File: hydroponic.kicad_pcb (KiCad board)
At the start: 2 copper layers, 110 x 80.3 mm, 102 parts, among them J1 12V DC, J10 Matrix key, J11 ds18b20, J12 ec, J13 bh1750, J14 dht11, J2 vi, J3 po, J4 pa, J5 pb, J6 vo, J7 fa, J8 lt, J9 lcd, U1 ULN2003, U10 LM324, U11 AMP4953, U12 AMP4953, U13 AMP4953, U14 LM324, U2 STM32duino, U3 LM2596T-5V, U4 AMP4953, U5 nodemcu, U6 LM1117-3.3, U7 AMP4953, U8 AMP4953, U9 AMP4953

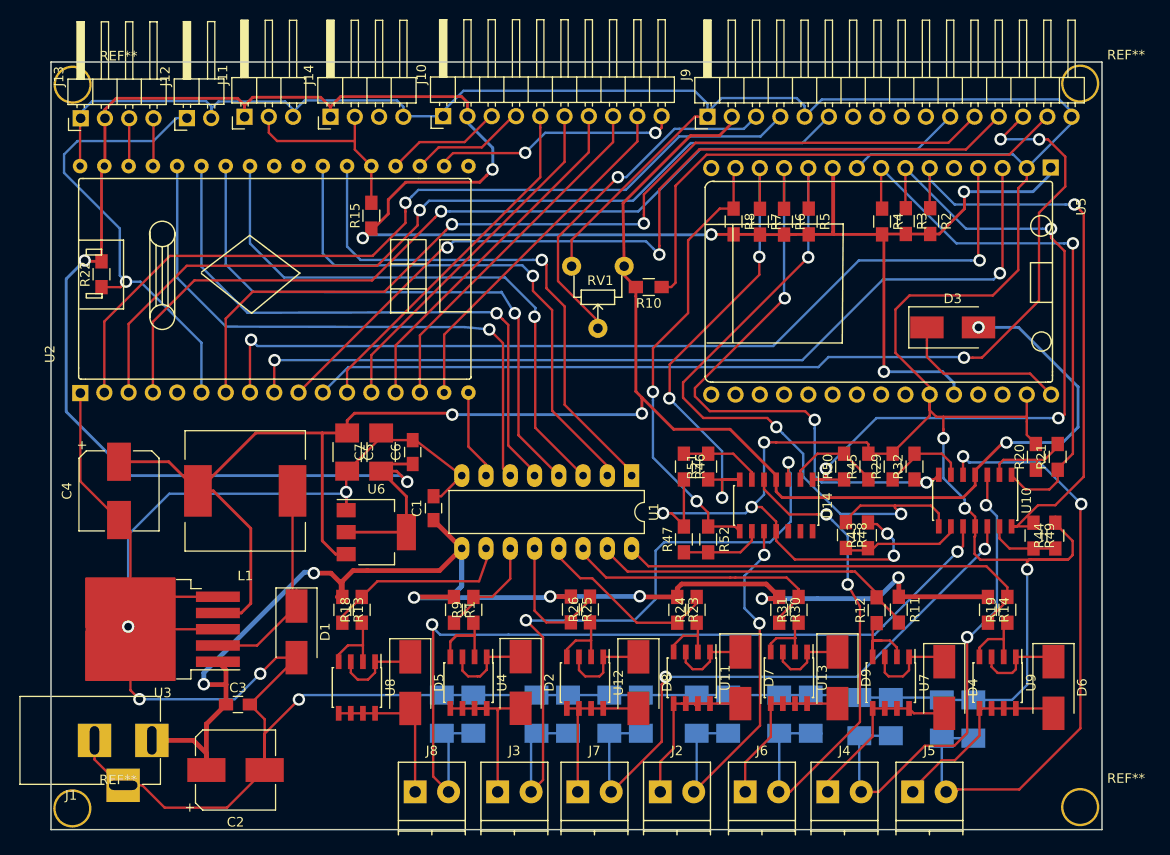
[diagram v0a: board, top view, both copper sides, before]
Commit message: add net 12v to AMP4953
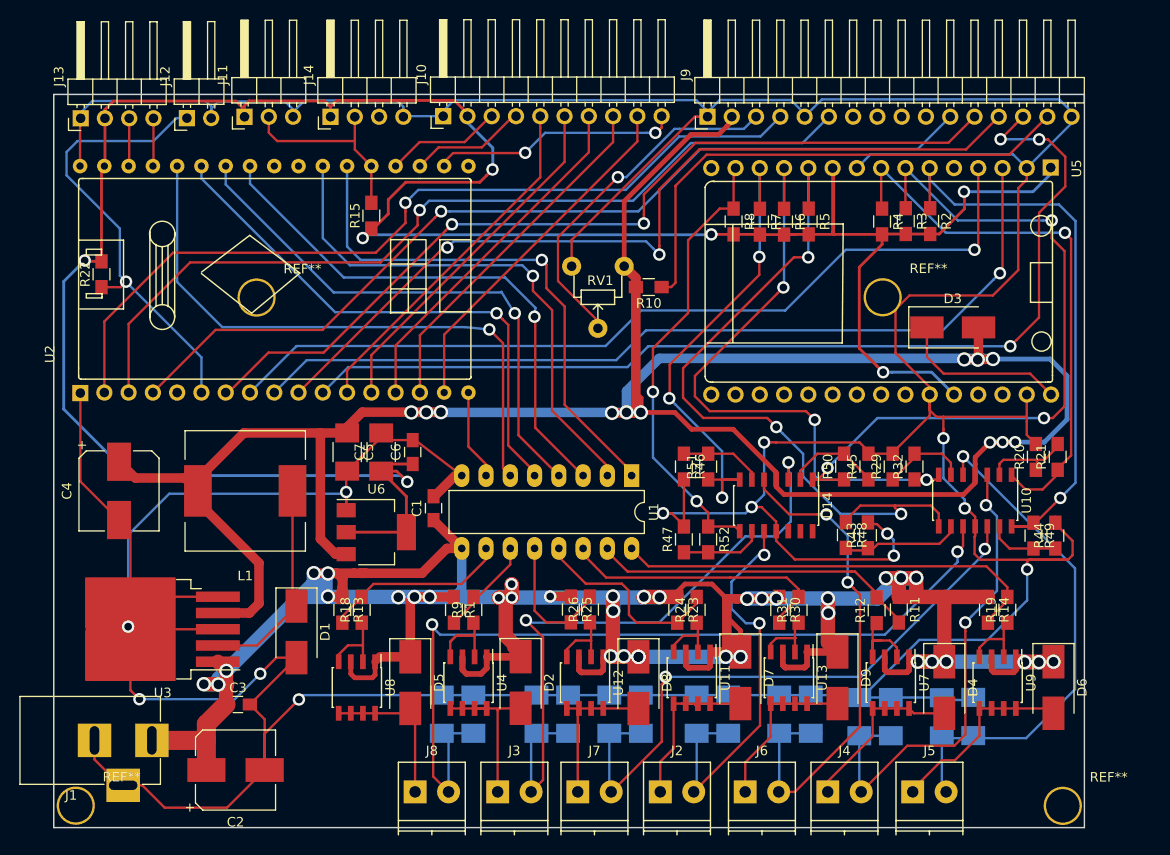
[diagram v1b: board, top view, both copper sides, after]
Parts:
- moved REF** 30.4 mm to (157.6, 87.2)
- moved REF** 29.4 mm to (92.1, 87.2)
- moved REF** 1.82 mm to (176.5, 140.4)
- moved REF** 0.46 mm to (73.2, 140.4)
- moved R28 0.27 mm to (167.1, 131.1)
- moved R27 0.24 mm to (163.8, 131.1)
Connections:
- D2 pad 1: Net-(D2-Pad1) -> +12V
- D4 pad 1: Net-(D4-Pad1) -> +12V
- D5 pad 1: Net-(D5-Pad1) -> +12V
- D6 pad 1: Net-(D6-Pad1) -> +12V
- D7 pad 1: Net-(D7-Pad1) -> +12V
- D8 pad 1: Net-(D8-Pad1) -> +12V
- D9 pad 1: Net-(D9-Pad1) -> +12V
- U11 pad 1: Net-(D7-Pad1) -> +12V
- U11 pad 3: Net-(D7-Pad1) -> +12V
- U12 pad 1: Net-(D8-Pad1) -> +12V
- U12 pad 3: Net-(D8-Pad1) -> +12V
- U13 pad 1: Net-(D9-Pad1) -> +12V
- U13 pad 3: Net-(D9-Pad1) -> +12V
- U4 pad 1: Net-(D2-Pad1) -> +12V
- U4 pad 3: Net-(D2-Pad1) -> +12V
- U7 pad 1: Net-(D4-Pad1) -> +12V
- U7 pad 3: Net-(D4-Pad1) -> +12V
- U8 pad 1: Net-(D5-Pad1) -> +12V
- U8 pad 3: Net-(D5-Pad1) -> +12V
- U9 pad 1: Net-(D6-Pad1) -> +12V
- U9 pad 3: Net-(D6-Pad1) -> +12V
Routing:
- net +12V: track 161.7 -> 434.1 mm, vias 7 -> 37
- net +5V: track 204.0 -> 319.3 mm, vias 4 -> 12
- net /PB_G: track 66.5 -> 53.7 mm, vias 2 -> 1
- net Net-(D5-Pad1): track 10.0 -> 0.00 mm
- net Net-(D4-Pad1): track 9.91 -> 0.00 mm
- net Net-(D8-Pad1): track 9.70 -> 0.00 mm
- net Net-(D6-Pad1): track 9.46 -> 0.00 mm
- net Net-(D2-Pad1): track 9.41 -> 0.00 mm
- net Net-(D7-Pad1): track 8.41 -> 0.00 mm
- net Net-(D9-Pad1): track 8.41 -> 0.00 mm
- net /FAN: track 62.1 -> 56.6 mm
- net /VI: track 62.0 -> 57.1 mm
- net /RX: track 95.5 -> 90.7 mm, vias 2 -> 1
- net /LCD_D5: track 97.3 -> 92.8 mm
- net /LCD_D4: track 100.1 -> 95.8 mm
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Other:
- board size 110 x 80.3 mm -> 107.8 x 76.7 mm
- net class 12V: trace_width 0.5 -> 0.6
- net class 5V: trace_width 0.3 -> 0.5

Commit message: edit all power in pcb
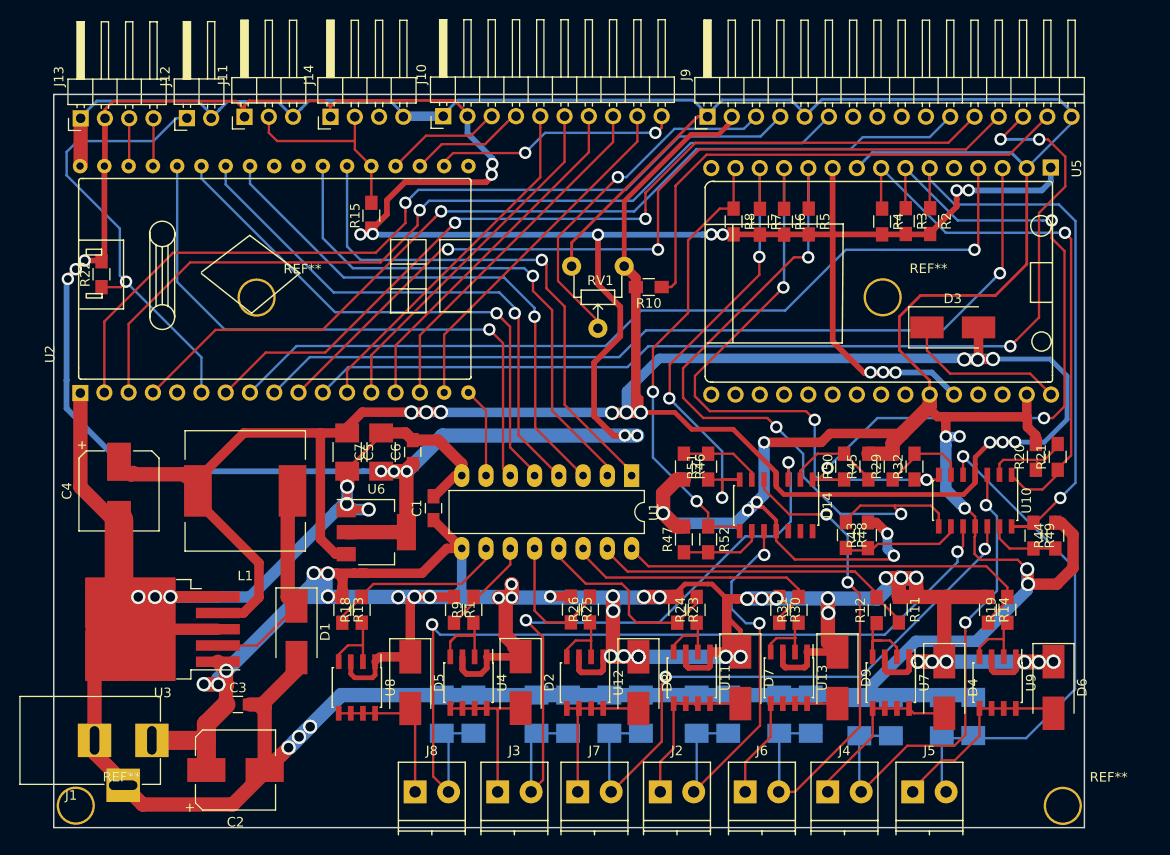
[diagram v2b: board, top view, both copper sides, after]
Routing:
- net +3V3: track 279.3 -> 413.4 mm, vias 7 -> 20
- net GND: track 607.4 -> 708.2 mm, vias 13 -> 20
- net /LCD_D6: track 91.0 -> 89.7 mm
- net /LCD_D5: track 92.8 -> 91.9 mm
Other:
- net class 3.3V: trace_width 0.3 -> 0.6
- net class Default: trace_width 0.25 -> 0.4

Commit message: edit all net in pcb
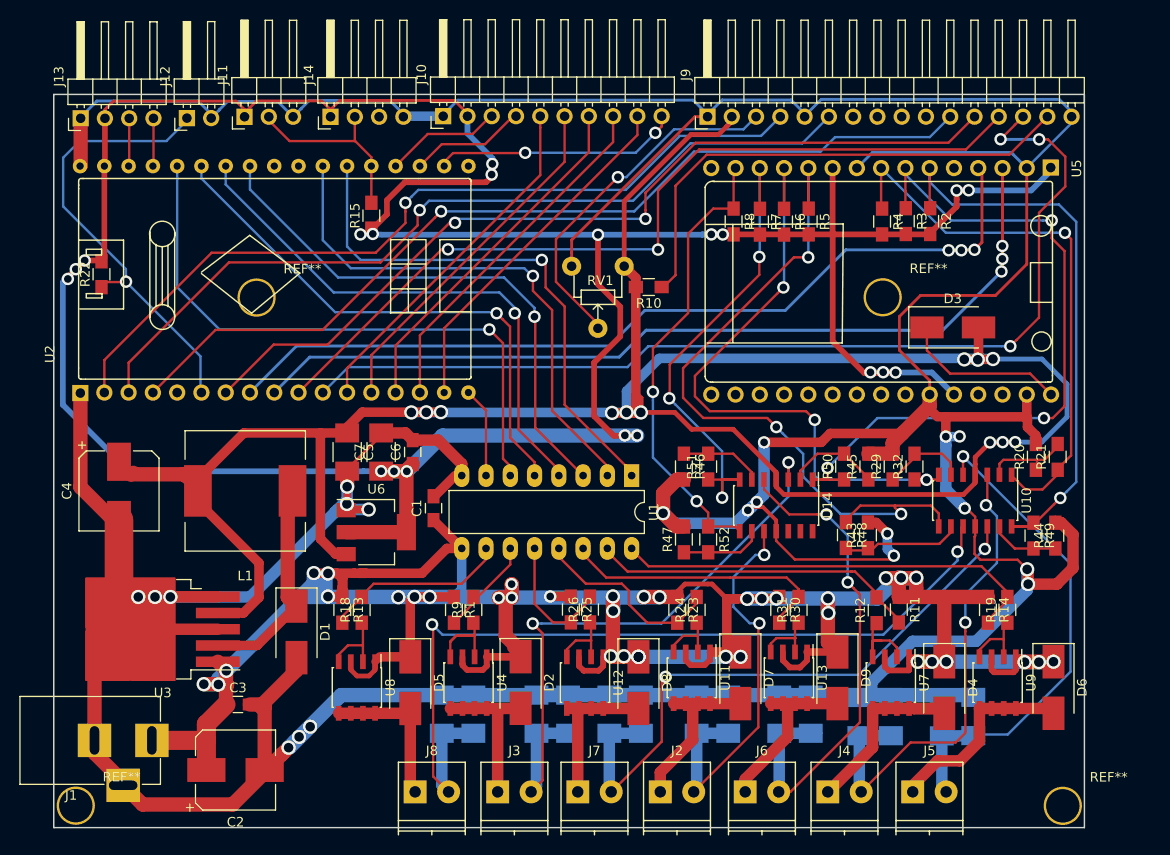
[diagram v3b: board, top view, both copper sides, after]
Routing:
- net /TX: track 92.2 -> 149.6 mm, vias 1 -> 3
- net +12V: track 434.1 -> 423.8 mm
- net GND: track 708.2 -> 700.1 mm
- net /VI-: track 17.5 -> 25.3 mm
- net /PB-: track 20.4 -> 28.2 mm
- net /PA-: track 18.4 -> 26.1 mm
- net /VO-: track 17.3 -> 25.0 mm
- net /PO-: track 17.0 -> 24.4 mm
- net /FAN-: track 16.3 -> 23.4 mm
- net /LIGHT-: track 16.6 -> 23.6 mm
- net /PB_G: track 53.7 -> 60.7 mm
- net /PO_G: track 70.8 -> 67.5 mm
- net /RX: track 90.7 -> 93.8 mm, vias 1 -> 3
- net /EN: track 90.3 -> 87.9 mm
- net /RS: track 88.3 -> 85.9 mm
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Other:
- net class Default: trace_width 0.4 -> 0.3

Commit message: add gerber file
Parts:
- removed C2: 100uF/50v, Capacitors_SMD:CP_Elec_8x10
- renumbered REF** to .
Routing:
- net Net-(R9-Pad1): track 10.6 -> 8.57 mm
- added copper zone on B.Cu, net GND
- added copper zone on F.Cu, net GND
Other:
- board text added: "Hydroponis_V1.0"
